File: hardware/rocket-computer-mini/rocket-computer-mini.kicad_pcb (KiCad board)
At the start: 6 copper layers, 22 x 54.8 mm, 150 parts, among them J2 TBLH11-350-05-BK, J3 JST_B2B-PH-SM4-TB, J6 USB4110GFA, J8 CON-SMA-EDGE-S, Q3 DTC123J, Q4 DTC123J, Q5 DTC123J, Q6 DTC123J, SW3 R-667995, U10 TPN4R712MD, U11 GD5F1GQ5UEYIGR, U13 GD25Q128ESIG, U14 479480001, U15 ESP32-S3RH2, U16 E220-900MM22S, U18 TPS62152RGTR, U2 ISM6HG256XTR, U21 TPS2121RUXR, U23 INA230AIRGTR, U3 IIS2MDCTR, U30 TPS22810DRVR, U4 BMP585, U5 LC86GLAMD, U6 TPN4R712MD, U7 TPN4R712MD, U8 TPN4R712MD, U9 CSD16323Q3, Y1 ABS07-32.768KHZ-T, Y2 ECS-400-10-37B2-CKY-TR

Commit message: hardware(minis): cost-reduction part swaps (Tier A + USB-C + QMC5883P)
rocket-computer-mini:
- pyro high-side P-FETs U6-U10: TPN4R712MD -> Winsok WSD20L50DN33 (incumbent
  unbuyable at build qty until the Q4-2026 Mouser restock; land compatibility
  closed by numeric overlay of the vendor package drawing vs the TSON Advance
  land vs the Toshiba outline -- identical 0.202 mm bottom-metal overlap;
  first-article gate: end-face wetting + bench-fire)
- pyro-ARM N-FET U9: CSD16323Q3 -> AOS AON7534 (same pinout, land verified)
- gate drivers Q3-Q6: DTC123JEBTL -> DTC123JETL (SOT-416 leads land fully)
- battery shunt R72: CSSH0805FT2L00 -> Yageo PA0805FRF870R002L
- magnetometer U3: IIS2MDC -> QST QMC5883P (new Custom symbol + LGA-16 3x3
  footprint from the vendor land; U3 relocated, C2/C4/C6 re-arranged; C6
  220 nF -> 4.7 uF 16 V 0603 for the C1 reservoir; 2x2 mm all-layer no-pour
  rule area under the die; stale X/Y axis silk removed -- new markings when
  the firmware axis mapping is decided; needs a new ~10-register driver)
- USB-C stays GCT: the HRO's through-hole shell legs land inside the pyro
  terminal's back-side SMD pads -- physically blocked at this location

base-station-mini:
- USB-C J2: GCT USB4110-GF-A -> HRO TYPE-C-31-M-12 (project footprint with
  symbol-matched pad names; NPTH-aligned placement, mating face within
  0.03 mm of the GCT; R14/R15 nudged 1.0 mm, one GND via moved, VBUS
  re-bridged; DRC 0 unconnected / 0 parity; shell-leg holes must be fully
  filled with solder at assembly)
- thermistor TH1: 103AT-2 -> MF52B 103F3435-100 (beta 3435 matched, charger
  TS window unchanged)
- LEDs D6/D9: Kingbright -> Xinglight

both minis:
- 22 uF 0805: CL21A226MOQNNNE -> CL21A226KOQNNNE (tighter K tolerance)
- bom.csv regenerated from the schematics; TSON footprint tags updated

Verification: rocket-mini ERC one error better than baseline, DRC 246
unconnected (3 better), parity equal, no new errors; base-mini ERC unchanged,
DRC clean.

Co-Authored-By: Cla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
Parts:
- C6: value 220 nF -> 4.7 uF; footprint Capacitor_SMD:C_0402_1005Metric -> Capacitor_SMD:C_0603_1608Metric
- U10, U6, U7, U8: value TPN4R712MD -> WSD20L50DN33
- U3: value IIS2MDCTR -> QMC5883P; footprint Footprints:LGA-12_2X2X0P7_STM -> Footprints:QMC5883P_LGA-16_3x3
- U9: value CSD16323Q3 -> AON7534
- moved C6 6.68 mm to (75.3, 164.0)
- moved C2 4.33 mm to (73.6, 165.8), turned to 90 degrees
- moved C4 2.94 mm to (74.8, 165.8), turned to 90 degrees
- moved U3 1.31 mm to (75.6, 168.8)
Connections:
- U3 pad 10: V_MCU_SWTCH -> Net-(U3-C1)
- U3 pad 11: unconnected-(U3-NC-Pad11) -> GND
- U3 pad 2: unconnected-(U3-NC-Pad2) -> V_MCU_SWTCH
- U3 pad 3: V_MCU_SWTCH -> unconnected-(U3-NC-Pad3)
- U3 pad 4: SEN_SDA -> unconnected-(U3-NC-Pad4)
- U3 pad 5: Net-(U3-C1) -> unconnected-(U3-NC-Pad5)
- U3 pad 6: GND -> unconnected-(U3-NC-Pad6)
- U3 pad 8: GND -> unconnected-(U3-NC-Pad8)
- U3 pad 9: V_MCU_SWTCH -> GND
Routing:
- net Net-(U3-C1): track 0.00 -> 4.56 mm
- net V_MCU_SWTCH: track 0.00 -> 1.59 mm, vias 0 -> 1
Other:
- board text removed: "X"
- board text removed: "Y"

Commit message: hardware(rocket-computer-mini): barometer BMP585 -> BMP581
Same BMP5 sensor API/register map, so no firmware change; SPI wiring maps
1:1 (SCK/SDI/SDO/CSB/INT; VDD+VDDIO on the switched sensor rail; three VSS
pins stacked at the old GND pin position so existing wires are untouched).

- new Custom:BMP581 symbol (shared lib + sheet cache)
- new footprint Footprints:BMP581_LGA-10_2x2 from the vendor land - the 581
  is an LGA-10 2.0x2.0 vs the 585's 9-pad 3.25x3.25, so U4's footprint is
  replaced in place; placement/routing tidy-up belongs to the layout pass
- trade-off taken on: no gel fill / liquid resistance; the baro drives
  apogee detection, so bench-compare noise vs a 585 at first article
- bom.csv regenerated

ERC unchanged vs pre-swap; DRC parity at baseline, no new errors.

Co-Authored-By: Claude Fable 5 <noreply@anthropic.com>
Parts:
- U4: value BMP585 -> BMP581; footprint Footprints:LGA9_BMP585_BOS -> Footprints:BMP581_LGA-10_2x2
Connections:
- U4 pad 1: SENS_SCLK -> V_MCU_SWTCH
- U4 pad 2: SENS_SDI -> SENS_SCLK
- U4 pad 3: SENS_SDO -> GND
- U4 pad 4: V_MCU_SWTCH -> SENS_SDI
- U4 pad 5: BMP585_INT -> SENS_SDO
- U4 pad 6: GND -> BMP585_CS
- U4 pad 7: BMP585_CS -> BMP585_INT
- U4 pad 8: V_MCU_SWTCH -> GND
- U4 pad 9: unconnected-(U4-L/M-Pad9) -> GND

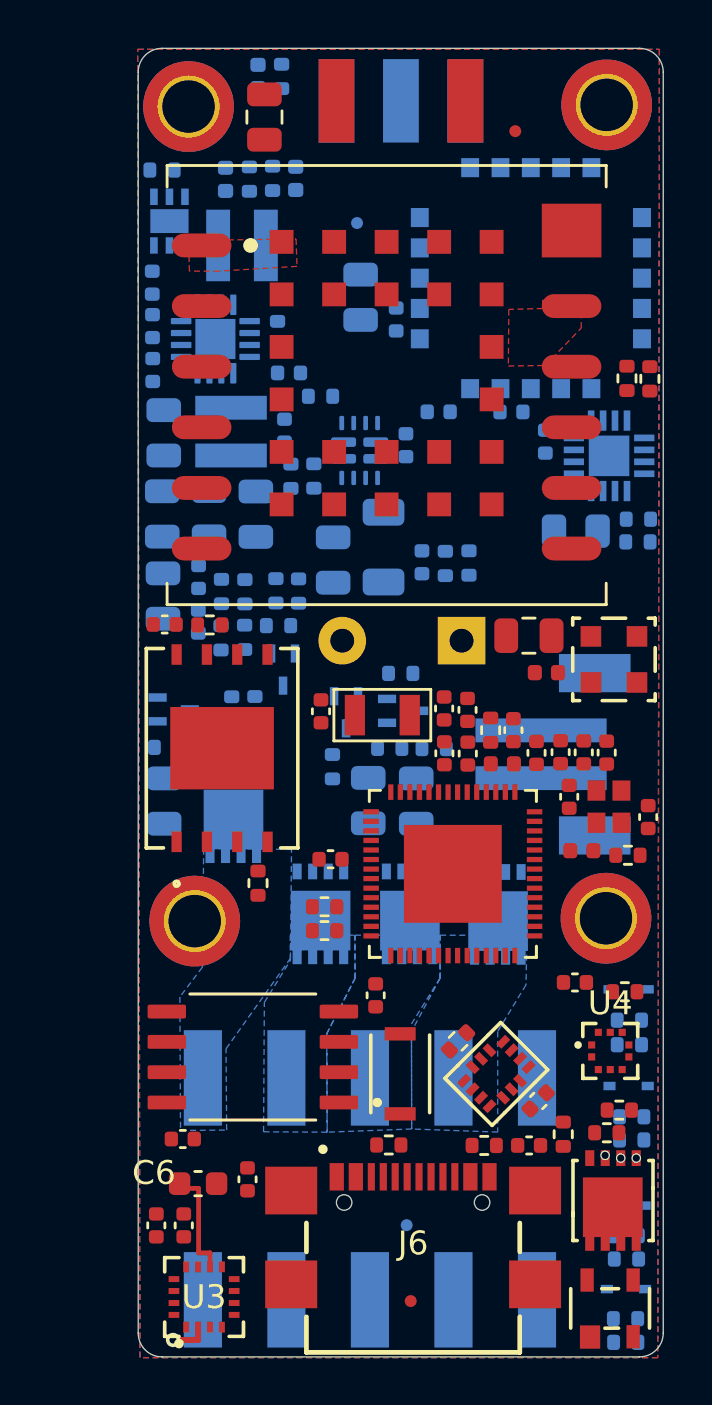
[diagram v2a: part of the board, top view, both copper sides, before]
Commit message: hardware(rocket-computer-mini): reconcile eFuse layout session with PR #797
The uncommitted eFuse placement session (C94/Q11/R85/U19 placed on B.Cu,
36 parts re-placed including an RF-corner rework, 164 tracks, 30 vias,
10 zones, one GND rewire on the power sheet) predated the PR #797 merge.
Reconciled by taking the session's files as the base and re-applying the
PR's scripted changes on top: U4 -> BMP581, the QMC5883P cluster
(U3/C2/C4/C6 + rule area + C1/VDD routes + stale axis silk removal), and
the cost-swap part fields (Winsok FETs, AON7534, DTC123JETL, PA0805,
K-code 22 uF caps).

Verification: netlist pad-net refresh needed zero corrections; BOM output
identical to the committed bom.csv; DRC 194 unconnected (best state yet),
schematic parity down to 1 item (the pre-existing U9 symbol-EP-pin-9 vs
footprint-pad-5 numbering; electrically covered - all drain pads carry
PYRO_GND). Known leftovers for layout review: two eFuse B.Cu tracks
crossing a session keepout (items_not_allowed), Y2/U19 lib-resave
mismatch warnings.

Co-Authored-By: Claude Fable 5 <noreply@anthropic.com>
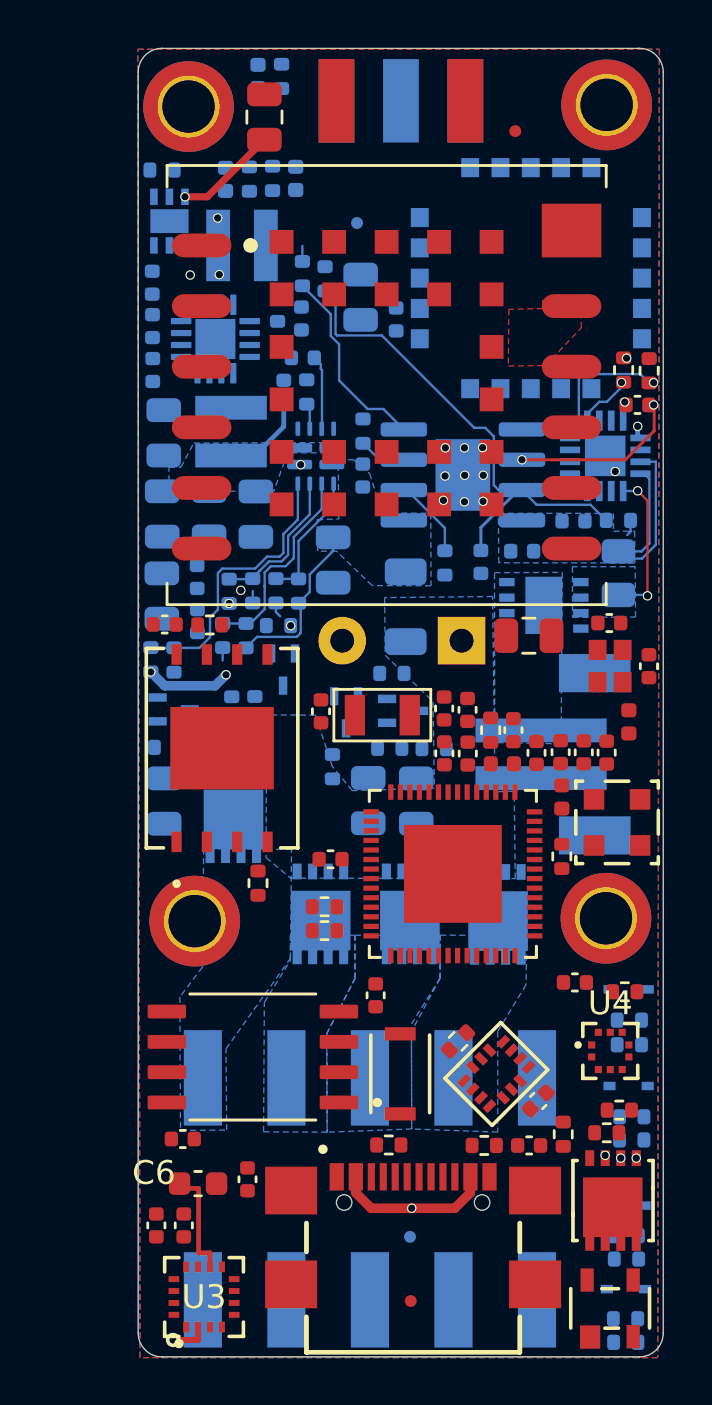
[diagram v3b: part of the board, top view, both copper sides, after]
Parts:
- added C94: 10 uF, Capacitor_SMD:C_0402_1005Metric, B.Cu at (87.2, 137.9)
- added Q11: AONR21321, Footprints:DFN-8-1EP_3x3mm_P0.65mm_EP1.55x2.4mm, B.Cu at (89.8, 139.8)
- added R85: 13.7 k, Resistor_SMD:R_0402_1005Metric, B.Cu at (79.7, 125.9)
- added U19: TPS259631DDAR, Footprints:SOIC-8-1EP_3.9x4.9mm_P1.27mm_EP2.29x3mm_ThermalVias, B.Cu at (86.4, 134.3)
- C51: moved to F.Cu
- moved R45 17.1 mm to (80.7, 126.1), turned to -90 degrees
- moved C51 11.2 mm to (93.8, 131.4), turned to 180 degrees
- moved R62 10.3 mm to (73.4, 142.1), turned to -90 degrees
- moved R63 9.13 mm to (74.3, 142.1), turned to 90 degrees
- moved C22 7.47 mm to (92.6, 140.5), turned to 0 degrees
- moved R48 7.09 mm to (82.3, 132.5), turned to -90 degrees
- moved U14 6.83 mm to (92.9, 148.9), turned to 90 degrees
- moved C20 6.32 mm to (94.2, 142.3)
- moved C52 6.12 mm to (79.7, 129.4), turned to 180 degrees
- moved Y2 5.89 mm to (92.6, 142.3)
- moved L3 5.75 mm to (93.4, 144.7), turned to -90 degrees
- moved C42 5.26 mm to (91.1, 136.2), turned to 0 degrees
- moved L1 5.25 mm to (90.6, 147.8), turned to -90 degrees
- moved C41 4.69 mm to (88.9, 137.5), turned to 180 degrees
- moved R37 2.77 mm to (90.6, 150.3), turned to -90 degrees
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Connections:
- R45 pad 1: GND -> Net-(U19-OVLO)
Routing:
- net Net-(J6-VBUS): track 0.00 -> 51.5 mm, vias 0 -> 5
- net +3V3: track 0.00 -> 27.2 mm, vias 0 -> 5
- net Net-(U19-EN/UVLO): track 0.00 -> 21.2 mm
- net Net-(U21-PR1): track 0.00 -> 11.7 mm
- net VBAT_CON: track 0.00 -> 11.0 mm
- net Net-(U21-OV2): track 0.00 -> 8.63 mm
- net Net-(U19-OVLO): track 0.00 -> 8.17 mm
- net VBATT: track 0.00 -> 7.19 mm
- net Net-(U19-dVdt): track 0.00 -> 7.14 mm, vias 0 -> 2
- net VBAT_Terminal: track 0.00 -> 6.42 mm, vias 0 -> 2
- net Net-(U21-OV1): track 0.00 -> 6.28 mm
- net SEN_SDA: track 0.00 -> 6.08 mm, vias 0 -> 1
- net Net-(U21-CP2): track 0.00 -> 5.55 mm
- net V_MCU_2S: track 0.00 -> 3.69 mm
- net Net-(U19-~{FLT}): track 0.00 -> 3.33 mm
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- added copper zone on B.Cu, net VBATT
- added copper zone on B.Cu, net VBAT_CON
- added copper zone on B.Cu, net VBAT_J8
- added copper zone on B.Cu, net VBAT_Terminal
- added copper zone on B.Cu, net V_CAP
- added copper zone on B.Cu, net V_MCU_2S
- removed copper zone on F.Cu, net Net-(L6-Pad1)

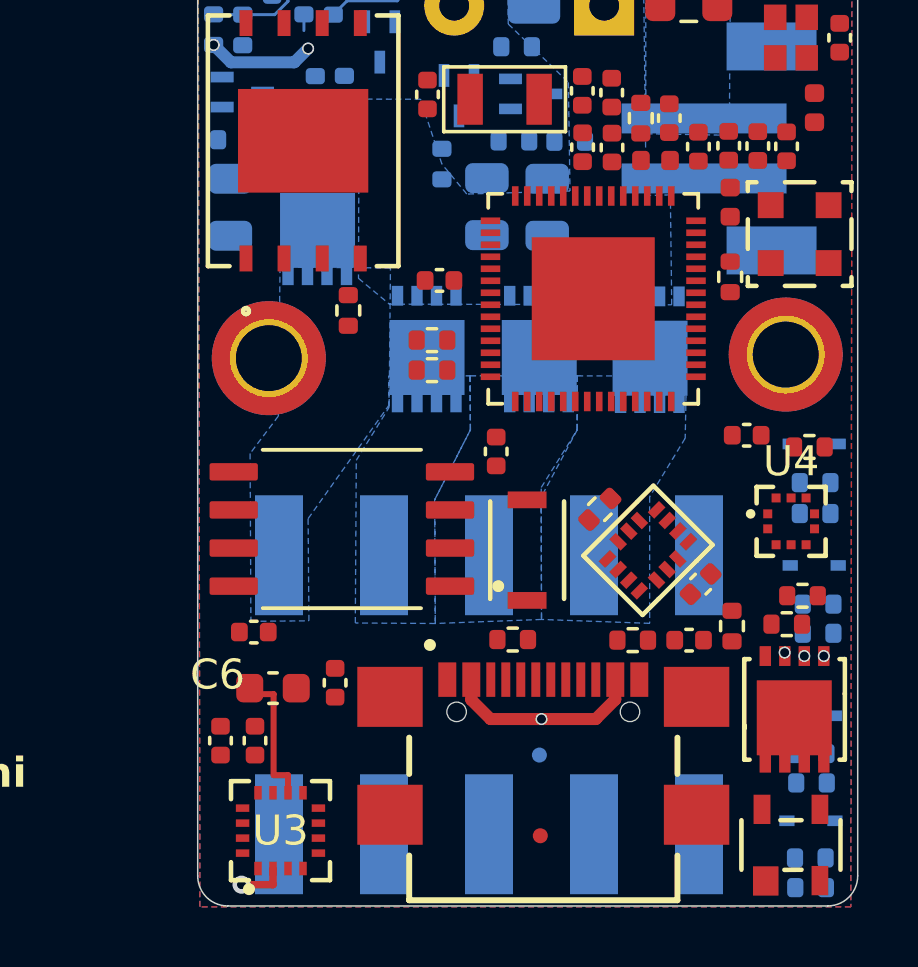
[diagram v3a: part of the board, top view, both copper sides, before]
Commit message: hardware(rocket-computer-mini): TDK chip antenna replaces the Molex BLE antenna
U14 (Molex 479480001, on-ground) removed; U31 (TDK ANT016008LCS2442MA2,
1.6x0.8 multilayer) is now the BLE antenna, placed per the layout session at
the bottom-right corner strip:

- keep-out: 2.9 x 6.5 mm all-layer rule area using the board's right and
  bottom edges as two sides (TDK asks 6 x 2.5); GND stitching vias along the
  west boundary
- printed radiator arm ~5.2 mm x 0.6 mm running down the right edge from the
  RAD pin (open end intentional - shows as one dangling-track warning)
- matching per TDK reference: L7 Ft 2.0 nH series + L8 Mt 3.0 nH shunt
  (LQG15 0402, EVAL VALUES - VNA tune on the real board required, S11
  < -10 dB across 2402-2480 MHz + range check vs a Molex board)
- feed: existing L1 4.3 nH shunt at the ESP32 stays; new ~15.5 mm 50-ohm
  stripline on In2 between the In1/In3 ground planes at 0.22 mm width
  (estimate for the default JLCPCB 6-layer JLC06161H-3313 stackup - VERIFY
  with JLCPCB's impedance calculator before ordering, or use their
  controlled-impedance service, In2 pour keep-out corridor, 2 vias with
  local ground return
- R21/R22/R37 relocated into the freed Molex area (clear of the H4 screw
  head courtyard and J3's back-side pads); redundant In2 GND stitching in
  the corridor removed
- C6 (QMC C1 reservoir) consolidated onto the stock 10 uF 0402 line per the
  owner's edit; the dedicated 4.7 uF line is gone
- schematic: ANT_FEED chain U15.RF + L1 -> Mt/Ft -> U31; U14 deleted

Verification: ERC 4 errors better than the session baseline; DRC zero new
errors, parity unchanged (1 pre-existing cosmetic), unconnected one better;
BOM reconciles with the curated cross-board sheet line-for-line. Known
cosmetics: radiator open-end dangling (by design), one 0.47 mm2 floating
In2 fill sliver (set zone island-removal or ignore), L7/L8 silk refs over
own pads.

Co-Authored-By: Claude Fable 5 <noreply@anthropic.com>
EOF
)
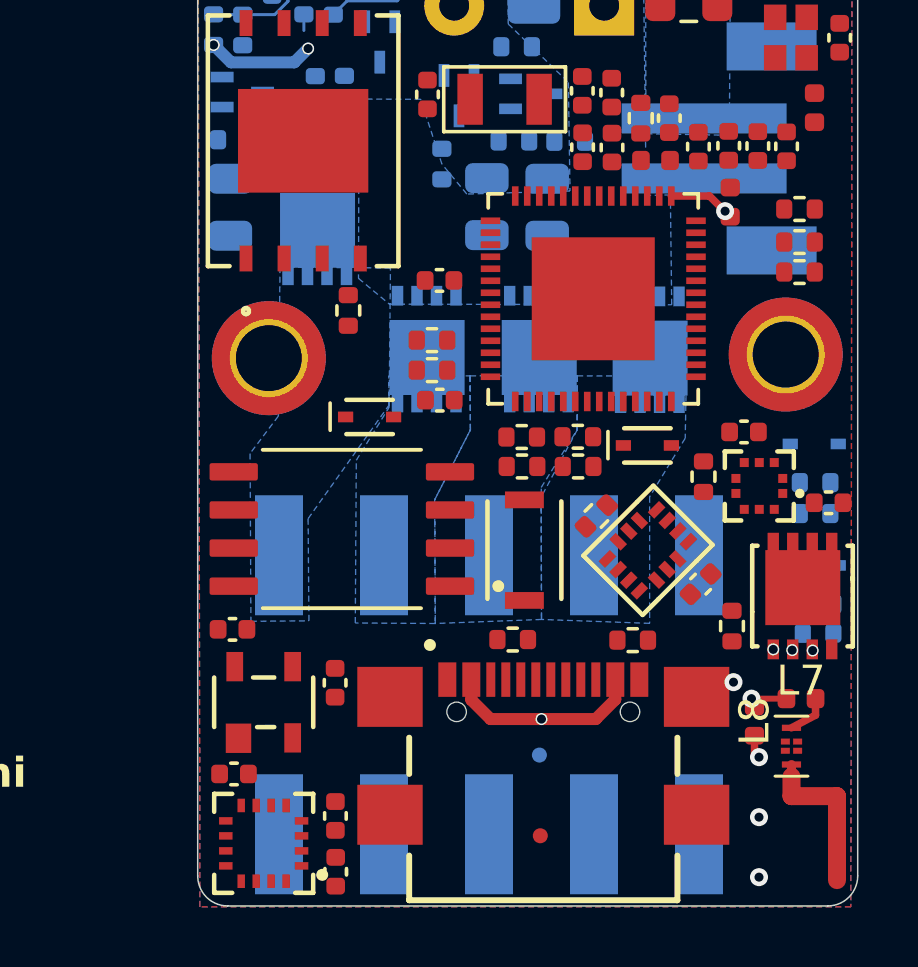
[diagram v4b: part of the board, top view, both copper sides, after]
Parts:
- removed U14: 479480001, Footprints:ANT_47948-0001_MOL
- added L7: 2 nH, Inductor_SMD:L_0402_1005Metric, F.Cu at (93.0, 164.3)
- added L8: 3 nH, Inductor_SMD:L_0402_1005Metric, F.Cu at (91.4, 165.1)
- added U31: ANT016008LCS2442MA2, Footprints:ANT016008LCS2442_TDK, F.Cu at (92.6, 165.9)
- C6: value 4.7 uF -> 10 uF; footprint Capacitor_SMD:C_0603_1608Metric -> Capacitor_SMD:C_0402_1005Metric
- D3, D4, R12, R13, R18, R19: moved to F.Cu
- moved CR3 18.2 mm to (75.0, 164.5)
- moved D3 17.7 mm to (78.6, 155.0)
- moved R18 16.9 mm to (85.5, 155.6)
- moved R19 15.2 mm to (85.5, 156.6), turned to 180 degrees
- moved R13 14.3 mm to (83.6, 155.6)
- moved R12 14.3 mm to (83.7, 156.6)
- moved D4 13.6 mm to (87.8, 155.9)
- moved R22 11.8 mm to (92.9, 149.1), turned to 0 degrees
- moved R21 11.7 mm to (92.9, 150.1)
- moved C5 6.53 mm to (93.9, 157.8)
- moved C2 5.82 mm to (77.4, 170.1), turned to -90 degrees
- moved U9 3.79 mm to (93.0, 160.9), turned to 90 degrees
- moved C4 3.67 mm to (77.4, 168.3)
- moved R4 3.67 mm to (89.7, 156.9), turned to 90 degrees
- moved R37 3.23 mm to (92.9, 148.0), turned to 0 degrees
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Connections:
- net Net-(U14-Feed) renamed /MCU - ESP32-S3/ANT_FEED
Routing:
- net /MCU - ESP32-S3/ANT_FEED: track 0.00 -> 21.4 mm, vias 0 -> 2
- net GND: track 32.5 -> 15.8 mm, vias 17 -> 21
- net unconnected-(U31-RAD-Pad1): track 0.00 -> 5.37 mm
- net Net-(U3-C1): track 4.56 -> 0.00 mm
- net V_MCU_SWTCH: track 1.59 -> 0.00 mm, vias 1 -> 0
- net Net-(U31-FEED): track 0.00 -> 1.46 mm

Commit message: hardware(rocket-computer-mini): two-sided TDK antenna pattern with tie vias
The TDK reference layout draws the printed radiator on BOTH outer layers,
joined by two vias inside the keep-out (their three layer views: pattern +
vias on top, cleared ground on the inner layer, a second 4.8 mm pattern with
the matching vias on the bottom). Those vias are part of the radiator, not
ground stitching - the earlier commit implemented the top half only, which
would have run electrically short and lossier than the characterised part.

- B.Cu mirror of the arm (4.72 mm, 0.6 mm wide) under the existing F.Cu arm
- 2 tie vias 4.27 mm apart (TDK: 4.2), inset 0.65 mm from the chip pad and
  0.45 mm from the open end; house 0.4/0.3 via in place of TDK's Phi0.2
- inner layers stay cleared by the existing all-layer keep-out; B.Cu inside
  the keep-out was empty, so nothing had to move
- far via sits 0.49 mm from the board edge

DRC: no new violations; the arm's dangling-end warning is resolved now that
it terminates into a via. Footprint description and the priced-BOM note
updated to record the two-sided requirement.

Co-Authored-By: Claude Fable 5 <noreply@anthropic.com>
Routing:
- net unconnected-(U31-RAD-Pad1): track 5.37 -> 10.1 mm, vias 0 -> 2
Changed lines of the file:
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@@
 			(at 0 -0.6 180)
 			(layer "F.SilkS")
+			(hide yes)
 			(effects
 				(font
@@
 			(at 0 1.17 0)
 			(layer "F.Fab")
+			(hide yes)
 			(effects
 				(font
@@
 			(at 0 0 90)
 			(layer "F.SilkS")
+			(hide yes)
 			(effects
 				(font
@@
 		)
 		(property "Value" "3 nH"
-			(at 0 1.17 270)
+			(at 0 1.17 90)
 			(layer "F.Fab")
+			(hide yes)
 			(effects
 				(font
@@
 		)
 		(property "Datasheet" ""
-			(at 0 0 270)
+			(at 0 0 90)
 			(layer "F.Fab")
 			(hide yes)
@@
 		)
 		(property "Description" "Inductor, small symbol"
-			(at 0 0 270)
+			(at 0 0 90)
 			(layer "F.Fab")
 			(hide yes)
@@
 		)
 		(property "MPN" "LQG15HS3N0S02D"
-			(at 0 0 270)
+			(at 0 0 90)
 			(layer "F.Fab")
 			(hide yes)
@@
 		)
 		(property "Mfr" "Murata"
-			(at 0 0 270)
+			(at 0 0 90)
 			(layer "F.Fab")
 			(hide yes)
@@
 		)
 		(property "KiLib_Generator" "SMD_2terminal_chip_molded"
-			(at 0 0 270)
+			(at 0 0 90)
 			(layer "F.SilkS")
 			(hide yes)
@@
 		)
 		(fp_text user "${REFERENCE}"
-			(at 0 0 270)
+			(at 0 0 90)
 			(layer "F.Fab")
 			(effects
@@
 		(net "unconnected-(U31-RAD-Pad1)")
 	)
+	(via
+		(at 94.15 169.95)
+		(size 0.4)
+		(drill 0.3)
+		(layers "F.Cu" "B.Cu")
+		(net "unconnected-(U31-RAD-Pad1)")
+	)
+	(via
+		(at 92.633 167.2)
+		(size 0.4)
+		(drill 0.3)
+		(layers "F.Cu" "B.Cu")
+		(net "unconnected-(U31-RAD-Pad1)")
+	)
+	(segment
+		(start 92.633 167.6)
+		(end 94.15 167.6)
+		(width 0.6)
+		(layer "B.Cu")
+		(net "unconnected-(U31-RAD-Pad1)")
+	)
+	(segment
+		(start 94.15 167.6)
+		(end 94.15 170.4)
+		(width 0.6)
+		(layer "B.Cu")
+		(net "unconnected-(U31-RAD-Pad1)")
+	)
+	(segment
+		(start 92.633 167.2)
+		(end 92.633 167.6)
+		(width 0.6)
+		(layer "B.Cu")
+		(net "unconnected-(U31-RAD-Pad1)")
+	)
